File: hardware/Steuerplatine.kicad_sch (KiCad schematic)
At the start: 7 parts, among them J1 Conn_01x02_Pin, J2 Conn_01x02_Pin

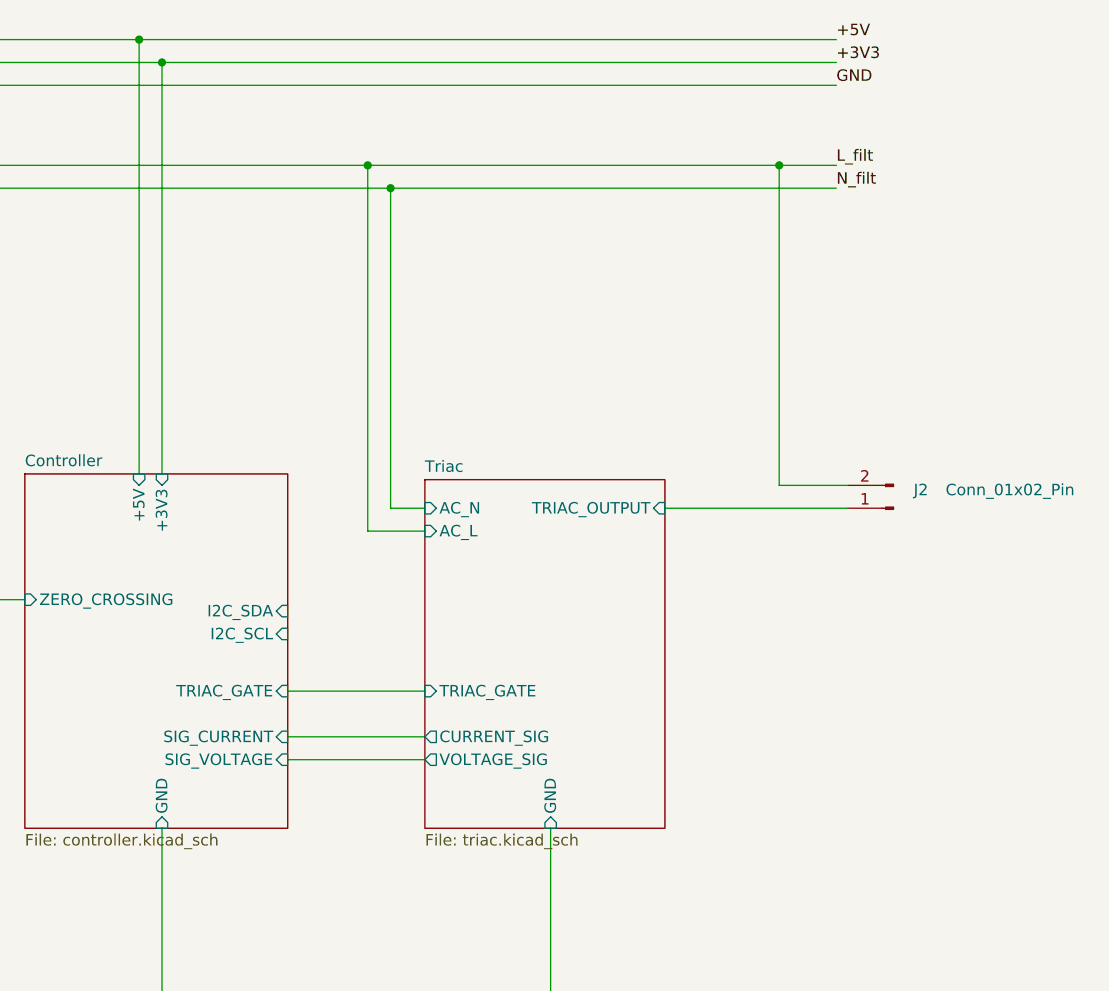
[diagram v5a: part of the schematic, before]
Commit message: added gnd layer
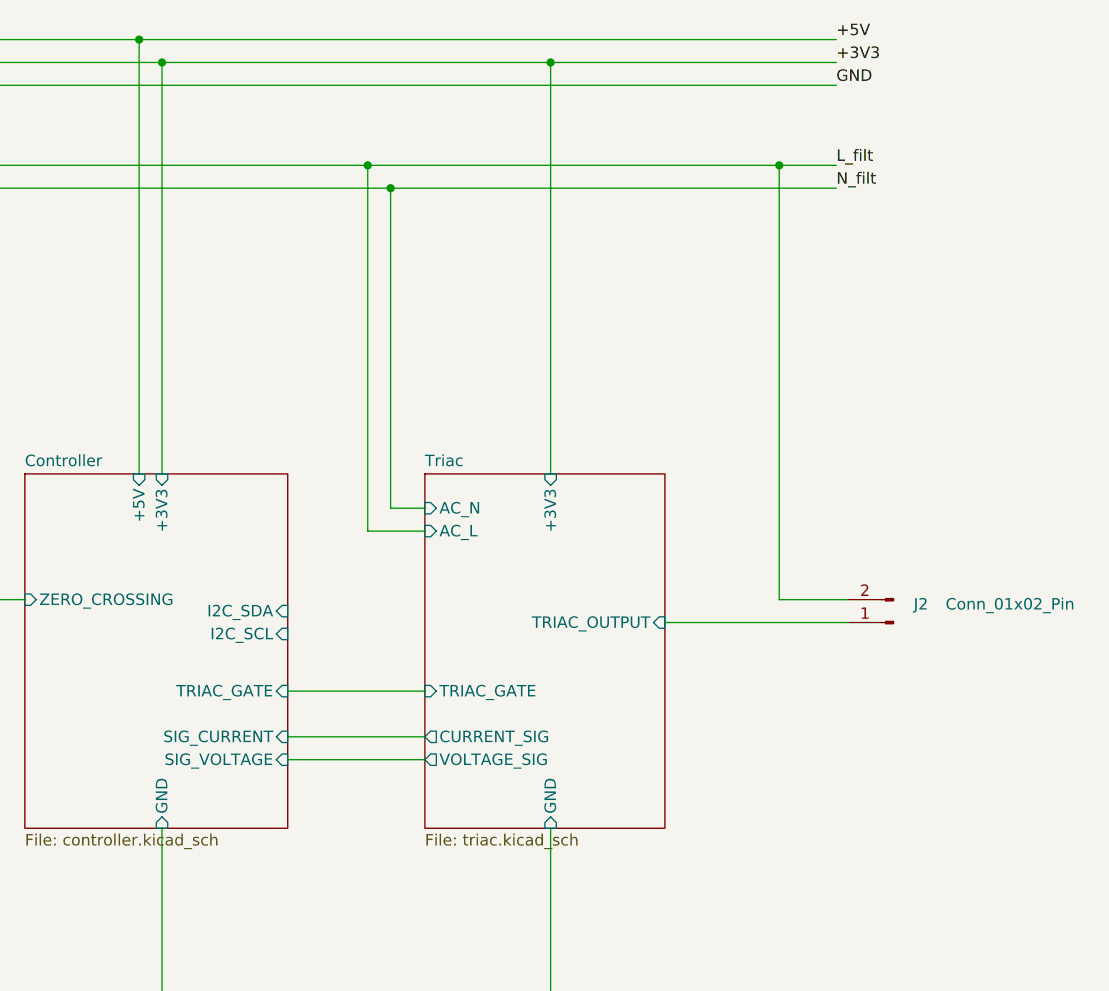
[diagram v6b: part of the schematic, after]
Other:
- sheet Triac ports: added +3V3; removed none
- moved on the sheet: J2
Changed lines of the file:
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@@
 		(color 0 0 0 0)
 	)
+	(junction
+		(at 219.71 24.13)
+		(diameter 0)
+		(color 0 0 0 0)
+	)
 	(wire
 		(pts
@@
 	(wire
 		(pts
-			(xy 176.53 24.13) (xy 251.46 24.13)
+			(xy 176.53 24.13) (xy 219.71 24.13)
 		)
 		(stroke
@@
 	(wire
 		(pts
-			(xy 232.41 73.66) (xy 252.73 73.66)
+			(xy 232.41 86.36) (xy 252.73 86.36)
 		)
 		(stroke
@@
 	(wire
 		(pts
+			(xy 219.71 24.13) (xy 219.71 69.85)
+		)
+		(stroke
+			(width 0)
+			(type default)
+		)
+	)
+	(wire
+		(pts
 			(xy 176.53 109.22) (xy 176.53 132.08)
 		)
@@
 	(wire
 		(pts
-			(xy 245.11 71.12) (xy 252.73 71.12)
+			(xy 245.11 83.82) (xy 252.73 83.82)
 		)
 		(stroke
@@
 	(wire
 		(pts
-			(xy 245.11 35.56) (xy 245.11 71.12)
+			(xy 245.11 35.56) (xy 245.11 83.82)
 		)
 		(stroke
@@
 		(pts
 			(xy 68.58 35.56) (xy 76.2 35.56)
+		)
+		(stroke
+			(width 0)
+			(type default)
+		)
+	)
+	(wire
+		(pts
+			(xy 219.71 24.13) (xy 251.46 24.13)
 		)
 		(stroke
@@
 	(symbol
 		(lib_id "Connector:Conn_01x02_Pin")
-		(at 257.81 73.66 180)
+		(at 257.81 86.36 180)
 		(unit 1)
 		(exclude_from_sim no)
@@
 		(dnp no)
 		(property "Reference" "J2"
-			(at 260.858 71.628 0)
+			(at 260.858 84.328 0)
 			(effects
 				(font
@@
 		)
 		(property "Value" "Conn_01x02_Pin"
-			(at 270.764 71.628 0)
+			(at 270.764 84.328 0)
 			(effects
 				(font
@@
 		)
 		(property "Footprint" "Connector_Phoenix_GMSTB:PhoenixContact_GMSTBA_2,5_2-G-7,62_1x02_P7.62mm_Horizontal"
-			(at 257.81 73.66 0)
+			(at 257.81 86.36 0)
 			(effects
 				(font
@@
 		)
 		(property "Datasheet" "~"
-			(at 257.81 73.66 0)
+			(at 257.81 86.36 0)
 			(effects
 				(font
@@
 		)
 		(property "Description" "Generic connector, single row, 01x02, script generated"
-			(at 257.81 73.66 0)
+			(at 257.81 86.36 0)
 			(effects
 				(font
@@
 	)
 	(sheet
-		(at 205.74 70.485)
-		(size 26.67 38.735)
+		(at 205.74 69.85)
+		(size 26.67 39.37)
 		(fields_autoplaced yes)
 		(stroke
@@
 		)
 		(property "Sheetname" "Triac"
-			(at 205.74 69.7734 0)
+			(at 205.74 69.1384 0)
 			(effects
 				(font
@@
 		)
 		(pin "TRIAC_OUTPUT" input
-			(at 232.41 73.66 0)
+			(at 232.41 86.36 0)
 			(effects
 				(font
@@
 			)
 		)
+		(pin "+3V3" input
+			(at 219.71 69.85 90)
+			(effects
+				(font
+					(size 1.27 1.27)
+				)
+				(justify right)
+			)
+		)

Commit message: changed opamp for a rail-to-rail device. bugfix: got the right package for phoenix mstba outlets. beauty: rearranged some test points for better visibility. bugfix: added bypass diodes to analog output to protect adc on chip
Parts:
- J1, J2: footprint Connector_Phoenix_GMSTB:PhoenixContact_GMSTBA_2,5_2-G-7,62_1x02_P7.62mm_Horizontal -> Connector_Phoenix_MSTB:PhoenixContact_MSTBA_2,5_2-G_1x02_P5.00mm_Horizontal
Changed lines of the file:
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@@
 			)
 		)
-		(property "Footprint" "Connector_Phoenix_GMSTB:PhoenixContact_GMSTBA_2,5_2-G-7,62_1x02_P7.62mm_Horizontal"
+		(property "Footprint" "Connector_Phoenix_MSTB:PhoenixContact_MSTBA_2,5_2-G_1x02_P5.00mm_Horizontal"
 			(at 257.81 86.36 0)
 			(effects
@@
 			)
 		)
-		(property "Footprint" "Connector_Phoenix_GMSTB:PhoenixContact_GMSTBA_2,5_2-G-7,62_1x02_P7.62mm_Horizontal"
+		(property "Footprint" "Connector_Phoenix_MSTB:PhoenixContact_MSTBA_2,5_2-G_1x02_P5.00mm_Horizontal"
 			(at 35.56 35.56 0)
 			(effects
